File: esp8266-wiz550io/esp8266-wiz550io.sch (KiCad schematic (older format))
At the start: 25 parts, among them J1 Conn_01x02, J2 Conn_01x04, J3 Conn_01x08, J4 Conn_01x06, J5 Conn_01x02, J6 Conn_01x03, J7 Conn_01x02, U1 ESP-12, U2 M74VHC1GT50DTT1G, U3 AP2112K-3.3

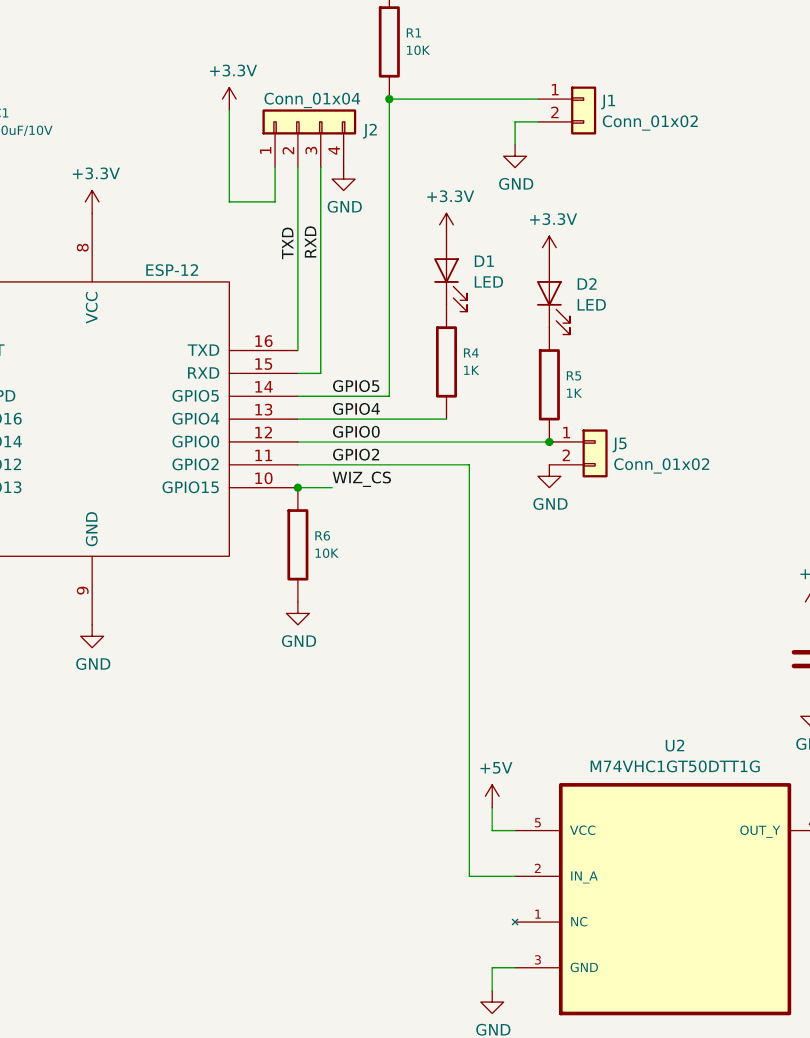
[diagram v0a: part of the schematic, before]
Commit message: esp8266-wiz550io: switch GPIO2 and GPIO4
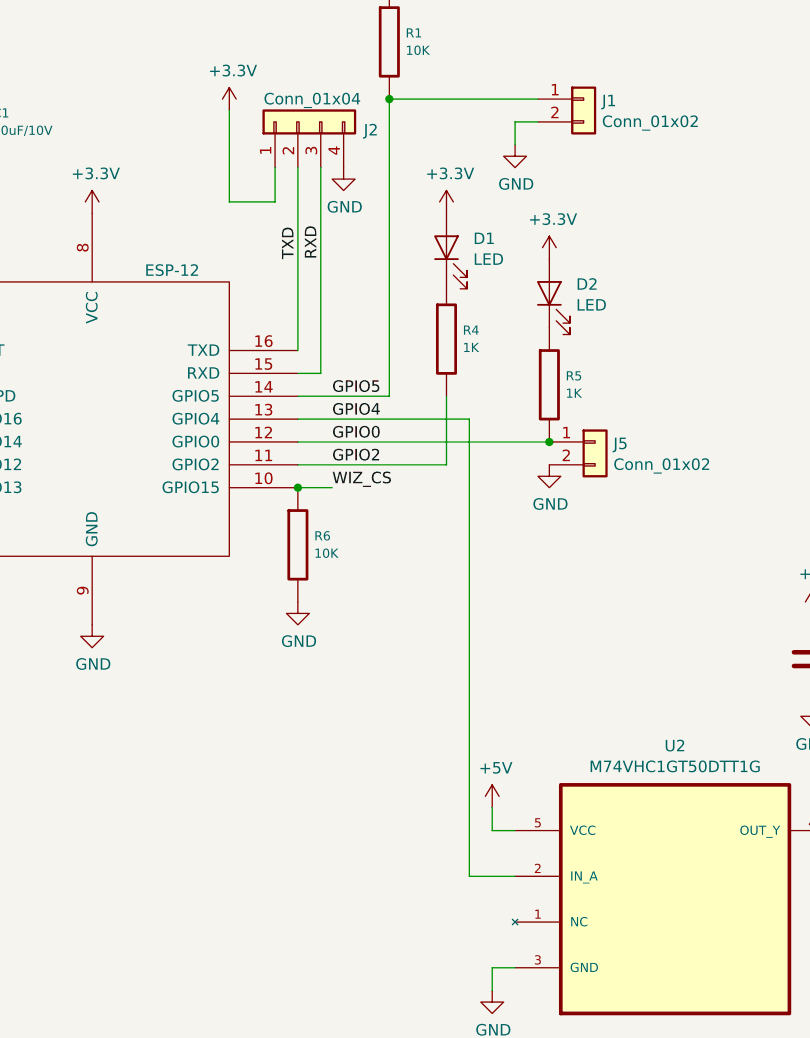
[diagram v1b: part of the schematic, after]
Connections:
- net GPIO2: now also R4.2; no longer U2.2 (IN_A)
- net GPIO4: now also U2.2 (IN_A); no longer R4.2
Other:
- moved on the sheet: D1, R4
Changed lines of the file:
@@
 L tom-passives:R R4
 U 1 1 5F737BF0
-P 8650 3550
-F 0 "R4" H 8721 3588 40  0000 L CNN
-F 1 "1K" H 8721 3512 40  0000 L CNN
-F 2 "tom-passives:C_0805_2012Metric" V 8580 3550 30  0001 C CNN
-F 3 "" H 8650 3550 30  0000 C CNN
-	1    8650 3550
+P 8650 3450
+F 0 "R4" H 8721 3488 40  0000 L CNN
+F 1 "1K" H 8721 3412 40  0000 L CNN
+F 2 "tom-passives:C_0805_2012Metric" V 8580 3450 30  0001 C CNN
+F 3 "" H 8650 3450 30  0000 C CNN
+	1    8650 3450
 	1    0    0    -1
 $EndComp
@@
 L power:+3.3V #PWR011
 U 1 1 5F73785F
-P 8650 3000
-F 0 "#PWR011" H 8650 2850 50  0001 C CNN
-F 1 "+3.3V" H 8665 3173 50  0000 C CNN
-F 2 "" H 8650 3000 50  0001 C CNN
-F 3 "" H 8650 3000 50  0001 C CNN
-	1    8650 3000
+P 8650 2900
+F 0 "#PWR011" H 8650 2750 50  0001 C CNN
+F 1 "+3.3V" H 8665 3073 50  0000 C CNN
+F 2 "" H 8650 2900 50  0001 C CNN
+F 3 "" H 8650 2900 50  0001 C CNN
+	1    8650 2900
 	1    0    0    -1
 $EndComp
@@
 L tom-opto:LED D1
 U 1 1 5F737272
-P 8650 3150
-F 0 "D1" V 8689 3033 50  0000 R CNN
-F 1 "LED" V 8598 3033 50  0000 R CNN
-F 2 "tom-opto:LED_0805_2012Metric" H 8650 3150 50  0001 C CNN
-F 3 "~" H 8650 3150 50  0001 C CNN
-	1    8650 3150
+P 8650 3050
+F 0 "D1" V 8689 2933 50  0000 R CNN
+F 1 "LED" V 8598 2933 50  0000 R CNN
+F 2 "tom-opto:LED_0805_2012Metric" H 8650 3050 50  0001 C CNN
+F 3 "~" H 8650 3050 50  0001 C CNN
+	1    8650 3050
 	0    -1   -1   0
 $EndComp
 Wire Wire Line
 	8000 3900 9100 3900
-Wire Wire Line
-	8000 3800 8650 3800
 Text Label 8000 3100 1    50   ~ 0
 TXD
@@
 Wire Wire Line
 	8950 5800 8750 5800
-Wire Wire Line
-	8750 5800 8750 4000
-Wire Wire Line
-	8000 4000 8750 4000
 $Comp
 L tom-passives:C C1
@@
 Wire Wire Line
 	4600 6250 4600 6350
+Wire Wire Line
+	8650 4000 8000 4000
+Wire Wire Line
+	8750 3800 8750 5800
+Wire Wire Line
+	8000 3800 8750 3800
+Wire Wire Line
+	8650 3700 8650 4000
 $EndSCHEMATC
